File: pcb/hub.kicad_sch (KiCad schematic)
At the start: 21 parts, among them U3 USB2514B, Y2 24MHz

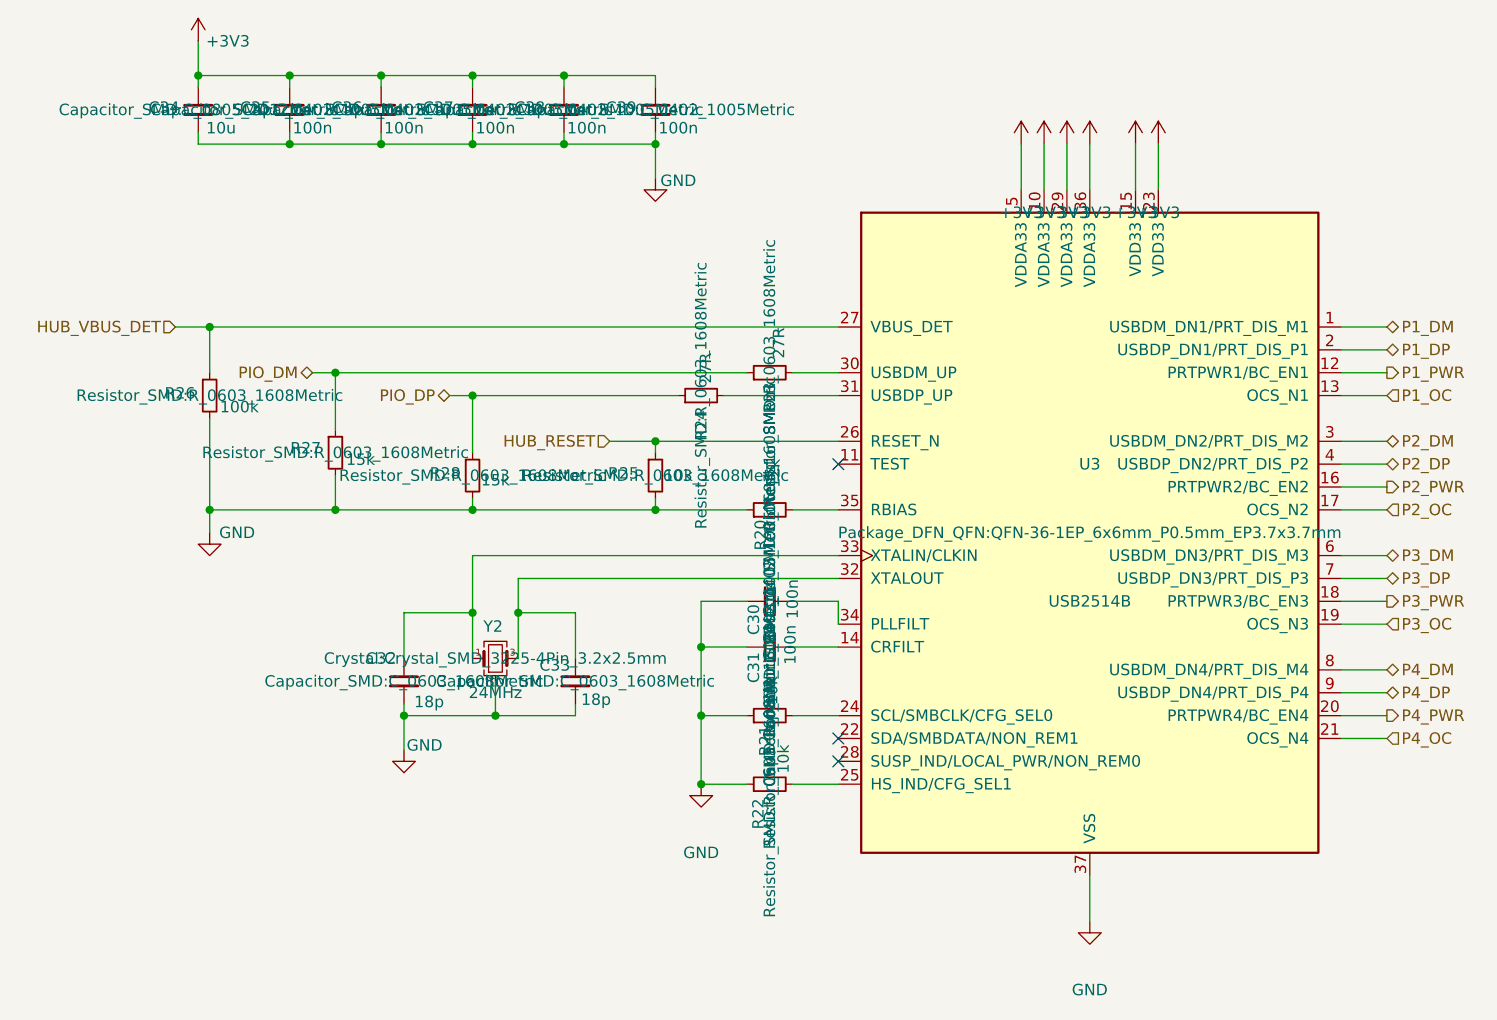
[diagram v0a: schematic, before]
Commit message: checkpoint the battery, PD and radio design as it stood
The last state of the full-featured board before it is reduced to a single
USB-C input: the power block re-placed part by part in order of importance,
the charger's signal pins fanned out, the differential pairs renamed so the
layout tool recognises them, the 3.3 V converter's feedback divider joined
to its pin, the FETs given their part number, and the non-printing fields
hidden on the schematic. The layout is incomplete and is recorded as such.

Co-Authored-By: Claude Fable 5.1 <noreply@anthropic.com>
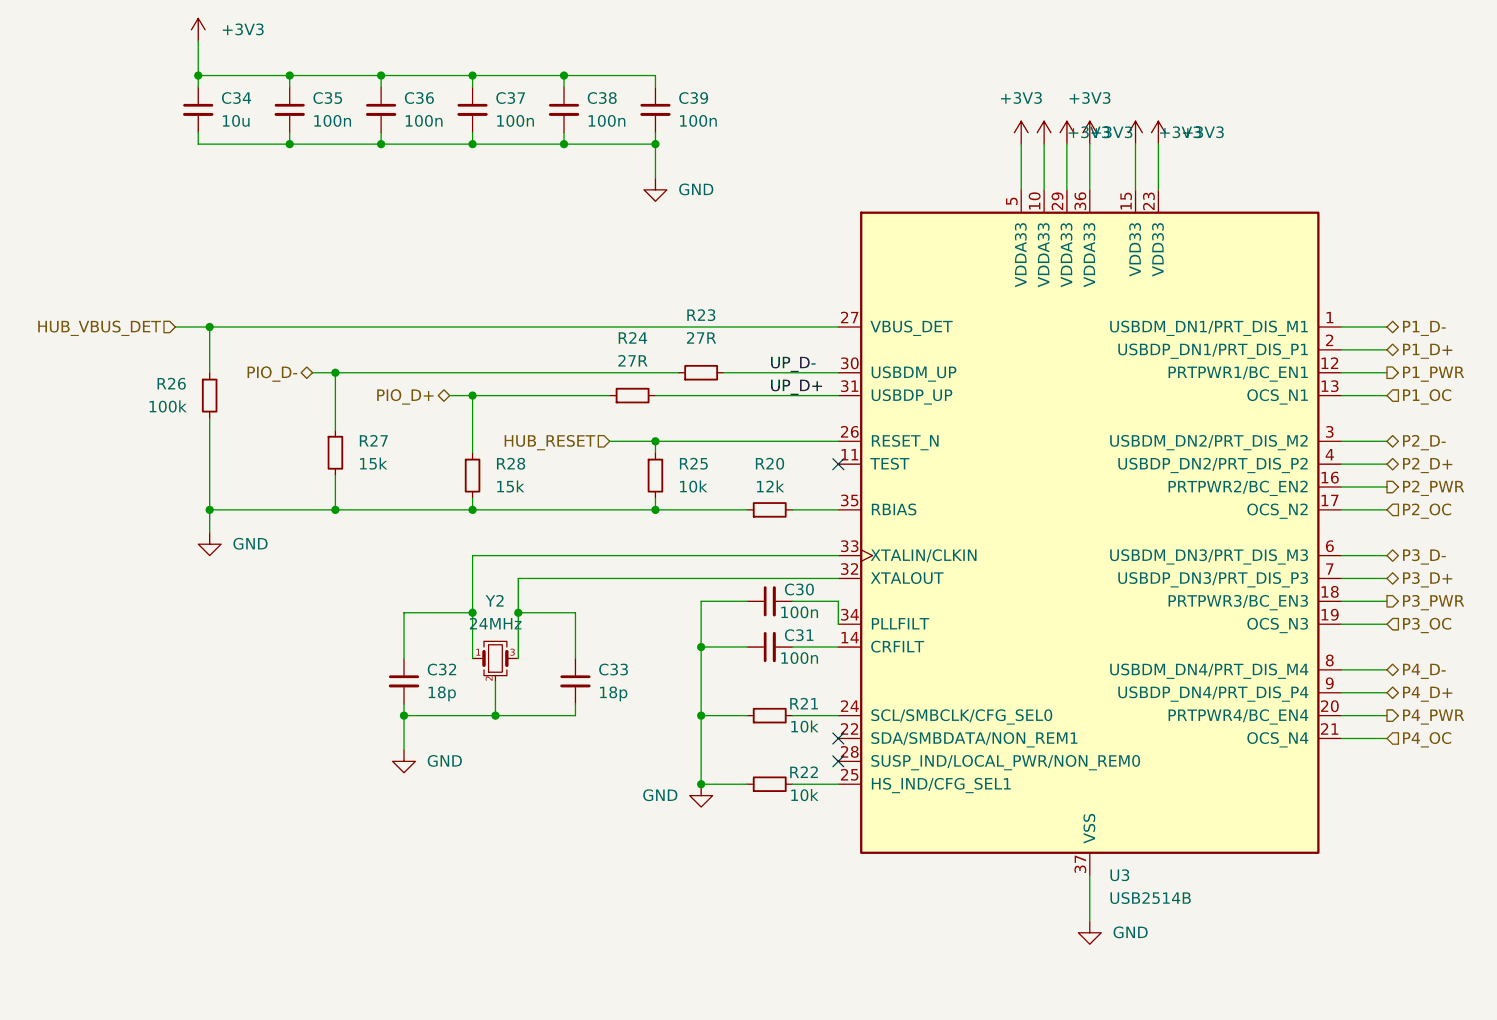
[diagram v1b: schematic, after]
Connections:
- net UP_D-: now reaches R23.2, U3.30 (USBDM_UP)
- net UP_D+: now reaches R24.2, U3.31 (USBDP_UP)
- net P1_DM renamed P1_D-
- net P1_DP renamed P1_D+
- net P2_DM renamed P2_D-
- net P2_DP renamed P2_D+
- net P3_DM renamed P3_D-
- net P3_DP renamed P3_D+
- net P4_DM renamed P4_D-
- net P4_DP renamed P4_D+
- net PIO_DM renamed PIO_D-
- net PIO_DP renamed PIO_D+
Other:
- moved on the sheet: R23, R24

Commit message: resistors to 0402
All nineteen, on the schematic and on the board, each keeping its identity,
position, face and nets; the placement is then rebuilt so the smaller parts
settle where they fit. The indicators stay 0603. Rules check clean; 39
items open, eighteen of them the pairs.

Co-Authored-By: Claude Fable 5.1 <noreply@anthropic.com>
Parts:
- R20, R21, R22, R23, R24, R25, R26, R27, R28: footprint Resistor_SMD:R_0603_1608Metric -> Resistor_SMD:R_0402_1005Metric
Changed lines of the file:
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@@
 			)
 		)
-		(property "Footprint" "Resistor_SMD:R_0603_1608Metric"
+		(property "Footprint" "Resistor_SMD:R_0402_1005Metric"
 			(at 167.64 147.32 0)
 			(hide yes)
@@
 			)
 		)
-		(property "Footprint" "Resistor_SMD:R_0603_1608Metric"
+		(property "Footprint" "Resistor_SMD:R_0402_1005Metric"
 			(at 105.41 111.76 0)
 			(hide yes)
@@
 			)
 		)
-		(property "Footprint" "Resistor_SMD:R_0603_1608Metric"
+		(property "Footprint" "Resistor_SMD:R_0402_1005Metric"
 			(at 160.02 109.22 0)
 			(hide yes)
@@
 			)
 		)
-		(property "Footprint" "Resistor_SMD:R_0603_1608Metric"
+		(property "Footprint" "Resistor_SMD:R_0402_1005Metric"
 			(at 167.64 154.94 0)
 			(hide yes)
@@
 			)
 		)
-		(property "Footprint" "Resistor_SMD:R_0603_1608Metric"
+		(property "Footprint" "Resistor_SMD:R_0402_1005Metric"
 			(at 119.38 118.11 0)
 			(hide yes)
@@
 			)
 		)
-		(property "Footprint" "Resistor_SMD:R_0603_1608Metric"
+		(property "Footprint" "Resistor_SMD:R_0402_1005Metric"
 			(at 152.4 111.76 0)
 			(hide yes)
@@
 			)
 		)
-		(property "Footprint" "Resistor_SMD:R_0603_1608Metric"
+		(property "Footprint" "Resistor_SMD:R_0402_1005Metric"
 			(at 167.64 124.46 0)
 			(hide yes)
@@
 			)
 		)
-		(property "Footprint" "Resistor_SMD:R_0603_1608Metric"
+		(property "Footprint" "Resistor_SMD:R_0402_1005Metric"
 			(at 154.94 120.65 0)
 			(hide yes)
@@
 			)
 		)
-		(property "Footprint" "Resistor_SMD:R_0603_1608Metric"
+		(property "Footprint" "Resistor_SMD:R_0402_1005Metric"
 			(at 134.62 120.65 0)
 			(hide yes)
